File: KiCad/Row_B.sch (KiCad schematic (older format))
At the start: 14 parts, among them U101 RGB_WS2811B, U102 RGB_WS2811B, U103 RGB_WS2811B, U104 RGB_WS2811B, U105 RGB_WS2811B, U106 RGB_WS2811B, U107 RGB_WS2811B, U108 RGB_WS2811B

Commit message: Schematic updated
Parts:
- removed C101: 100n, TinyTiM_Lib:c_0805, symbol C2
- removed C117: 47u,8V, TinyTiM_Lib:c_2917, symbol C_POL_1
- removed S101, S102, S103, S104: CONN_1, TinyTiM_Lib:Screw, symbol CONN_1
- removed U101, U102, U103, U104, U105, U106, U107, U108: RGB_WS2811B, TinyTiM_Lib:RGB_WS2811B, symbol RGB_WS2811B
- added C18, C19, C20, C21, C22, C23, C24, C25, C26, C27, C28, C29, C30, C31: 100n, TinyTiM_Lib:c_0805, symbol C2
- added U17, U18, U19, U20, U21, U22, U23, U24, U25, U26, U27, U28, U29, U30: RGB_WS2812B, symbol RGB_WS2812B
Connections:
- net labels added: DI_B, DO_B
- net labels removed: A_02, A_03, A_04, A_05, A_06, A_07, A_08, A_09, DI_A, DO_A
- wire segments 49 -> 82
- no-connect marks 4 -> 0
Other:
- note removed: "Mounting Screws"

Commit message: Schematic updated
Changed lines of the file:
@@
 Sheet 3 14
 Title "ClockFOUR"
-Date "29 sep 2014"
+Date "30 sep 2014"
 Rev ""
 Comp "WyoLum"
@@
 5V
 $Comp
-L GND #PWR7
+L GND #PWR013
 U 1 1 542A9B80
 P 1350 2350
-F 0 "#PWR7" H 1350 2350 30  0001 C CNN
+F 0 "#PWR013" H 1350 2350 30  0001 C CNN
 F 1 "GND" H 1350 2280 30  0001 C CNN
 F 2 "" H 1350 2350 60  0001 C CNN
@@
 	1450 2300 1450 4650
 Wire Wire Line
-	1450 4650 10400 4650
-Wire Wire Line
 	2000 4650 2000 4550
 Wire Wire Line
@@
 Connection ~ 2000 4650
 Wire Wire Line
-	9000 4650 9000 4550
-Connection ~ 9000 4650
-Wire Wire Line
 	7600 4650 7600 4550
 Connection ~ 7600 4650
-Wire Wire Line
-	6200 4650 6200 4550
-Connection ~ 6200 4650
 Wire Wire Line
 	4800 4650 4800 4550
@@
 Connection ~ 3300 5050
 Connection ~ 3300 4650
+Connection ~ 10200 5050
+Connection ~ 10400 4650
+Wire Wire Line
+	9000 4550 9000 4650
+Connection ~ 9000 4650
+Wire Wire Line
+	1450 4650 10400 4650
+Wire Wire Line
+	6200 4550 6200 4650
+Connection ~ 6200 4650
+Connection ~ 1450 2300
 $EndSCHEMATC

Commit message: Schematic updated, board started
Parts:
- C25: renamed from C18; Field5 100nF, 25V -> 100n, 25V
- C27: renamed from C22; Field5 100nF, 25V -> 100n, 25V
- C29: renamed from C26; Field5 100nF, 25V -> 100n, 25V
- C31: renamed from C30; Field5 100nF, 25V -> 100n, 25V
- C33: renamed from C21; Field5 100nF, 25V -> 100n, 25V
- C35: renamed from C25; Field5 100nF, 25V -> 100n, 25V
- C37: renamed from C29; Field5 100nF, 25V -> 100n, 25V
- renumbered C20 to C26, C24 to C28, C28 to C30, C19 to C32, C23 to C34, C27 to C36, C31 to C38, U17 to U16, U19 to U17, U21 to U18, U23 to U19, U25 to U20, U27 to U21, U29 to U22, U18 to U23, U20 to U24, U22 to U25, U24 to U26, U26 to U27, U30 to U29
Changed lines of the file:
@@
 LIBS:contrib
 LIBS:valves
-LIBS:TinyTiM-cache
-LIBS:TiNA_sym
+LIBS:ClockFOUR
 LIBS:ClockFOUR-cache
 EELAYER 27 0
@@
 Sheet 3 14
 Title "ClockFOUR"
-Date "30 sep 2014"
+Date "1 oct 2014"
 Rev ""
 Comp "WyoLum"
@@
 5V
 $Comp
-L GND #PWR013
+L GND #PWR015
 U 1 1 542A9B80
 P 1350 2350
-F 0 "#PWR013" H 1350 2350 30  0001 C CNN
+F 0 "#PWR015" H 1350 2350 30  0001 C CNN
 F 1 "GND" H 1350 2280 30  0001 C CNN
 F 2 "" H 1350 2350 60  0001 C CNN
@@
 $EndComp
 $Comp
-L C2 C18
+L C2 C25
 U 1 1 542A9B8E
 P 1900 2500
-F 0 "C18" H 1925 2600 50  0000 L CNN
+F 0 "C25" H 1925 2600 50  0000 L CNN
 F 1 "100n" H 1925 2400 50  0000 L CNN
 F 2 "TinyTiM_Lib:c_0805" H 1900 2500 50  0001 C CNN
 F 3 "" H 1900 2500 60  0001 C CNN
 F 4 "CAP CER 0.1UF 25V 10% X7R 0805" H 1900 2700 60  0001 L CNN "Field4"
-F 5 "100nF, 25V" H 1900 2800 60  0001 L CNN "Field5"
+F 5 "100n, 25V" H 1900 2800 60  0001 L CNN "Field5"
 F 6 "Surface Mount, MLCC" H 1900 2900 60  0001 L CNN "Field6"
 F 7 "Kemet" H 1900 3000 60  0001 L CNN "Field7"
@@
 $EndComp
 $Comp
-L RGB_WS2812B U17
+L RGB_WS2812B U16
 U 1 1 542A9B94
 P 1725 1525
-F 0 "U17" V 1475 1525 60  0000 C CNN
+F 0 "U16" V 1475 1525 60  0000 C CNN
 F 1 "RGB_WS2812B" V 2125 1525 60  0000 C CNN
 F 2 "" H 1725 1525 60  0000 C CNN
@@
 $EndComp
 $Comp
-L RGB_WS2812B U19
+L RGB_WS2812B U17
 U 1 1 542A9B9A
 P 3125 1525
-F 0 "U19" V 2875 1525 60  0000 C CNN
+F 0 "U17" V 2875 1525 60  0000 C CNN
 F 1 "RGB_WS2812B" V 3525 1525 60  0000 C CNN
 F 2 "" H 3125 1525 60  0000 C CNN
@@
 $EndComp
 $Comp
-L RGB_WS2812B U21
+L RGB_WS2812B U18
 U 1 1 542A9BA0
 P 4525 1525
-F 0 "U21" V 4275 1525 60  0000 C CNN
+F 0 "U18" V 4275 1525 60  0000 C CNN
 F 1 "RGB_WS2812B" V 4925 1525 60  0000 C CNN
 F 2 "" H 4525 1525 60  0000 C CNN
@@
 $EndComp
 $Comp
-L RGB_WS2812B U23
+L RGB_WS2812B U19
 U 1 1 542A9BA6
 P 5925 1525
-F 0 "U23" V 5675 1525 60  0000 C CNN
+F 0 "U19" V 5675 1525 60  0000 C CNN
 F 1 "RGB_WS2812B" V 6325 1525 60  0000 C CNN
 F 2 "" H 5925 1525 60  0000 C CNN
@@
 $EndComp
 $Comp
-L RGB_WS2812B U25
+L RGB_WS2812B U20
 U 1 1 542A9BAC
 P 7325 1525
-F 0 "U25" V 7075 1525 60  0000 C CNN
+F 0 "U20" V 7075 1525 60  0000 C CNN
 F 1 "RGB_WS2812B" V 7725 1525 60  0000 C CNN
 F 2 "" H 7325 1525 60  0000 C CNN
@@
 $EndComp
 $Comp
-L RGB_WS2812B U27
+L RGB_WS2812B U21
 U 1 1 542A9BB2
 P 8725 1525
-F 0 "U27" V 8475 1525 60  0000 C CNN
+F 0 "U21" V 8475 1525 60  0000 C CNN
 F 1 "RGB_WS2812B" V 9125 1525 60  0000 C CNN
 F 2 "" H 8725 1525 60  0000 C CNN
@@
 $EndComp
 $Comp
-L RGB_WS2812B U29
+L RGB_WS2812B U22
 U 1 1 542A9BB8
 P 10125 1525
-F 0 "U29" V 9875 1525 60  0000 C CNN
+F 0 "U22" V 9875 1525 60  0000 C CNN
 F 1 "RGB_WS2812B" V 10525 1525 60  0000 C CNN
 F 2 "" H 10125 1525 60  0000 C CNN
@@
 $EndComp
 $Comp
-L RGB_WS2812B U18
+L RGB_WS2812B U23
 U 1 1 542A9BBE
 P 1725 3925
-F 0 "U18" V 1475 3925 60  0000 C CNN
+F 0 "U23" V 1475 3925 60  0000 C CNN
 F 1 "RGB_WS2812B" V 2125 3925 60  0000 C CNN
 F 2 "" H 1725 3925 60  0000 C CNN
@@
 $EndComp
 $Comp
-L RGB_WS2812B U20
+L RGB_WS2812B U24
 U 1 1 542A9BC4
 P 3125 3925
-F 0 "U20" V 2875 3925 60  0000 C CNN
+F 0 "U24" V 2875 3925 60  0000 C CNN
 F 1 "RGB_WS2812B" V 3525 3925 60  0000 C CNN
 F 2 "" H 3125 3925 60  0000 C CNN
@@
 $EndComp
 $Comp
-L RGB_WS2812B U22
+L RGB_WS2812B U25
 U 1 1 542A9BCA
 P 4525 3925
-F 0 "U22" V 4275 3925 60  0000 C CNN
+F 0 "U25" V 4275 3925 60  0000 C CNN
 F 1 "RGB_WS2812B" V 4925 3925 60  0000 C CNN
 F 2 "" H 4525 3925 60  0000 C CNN
@@
 $EndComp
 $Comp
-L RGB_WS2812B U24
+L RGB_WS2812B U26
 U 1 1 542A9BD0
 P 5925 3925
-F 0 "U24" V 5675 3925 60  0000 C CNN
+F 0 "U26" V 5675 3925 60  0000 C CNN
 F 1 "RGB_WS2812B" V 6325 3925 60  0000 C CNN
 F 2 "" H 5925 3925 60  0000 C CNN
@@
 $EndComp
 $Comp
-L RGB_WS2812B U26
+L RGB_WS2812B U27
 U 1 1 542A9BD6
 P 7325 3925
-F 0 "U26" V 7075 3925 60  0000 C CNN
+F 0 "U27" V 7075 3925 60  0000 C CNN
 F 1 "RGB_WS2812B" V 7725 3925 60  0000 C CNN
 F 2 "" H 7325 3925 60  0000 C CNN
@@
 $EndComp
 $Comp
-L RGB_WS2812B U30
+L RGB_WS2812B U29
 U 1 1 542A9BE2
 P 10125 3925
-F 0 "U30" V 9875 3925 60  0000 C CNN
+F 0 "U29" V 9875 3925 60  0000 C CNN
 F 1 "RGB_WS2812B" V 10525 3925 60  0000 C CNN
 F 2 "" H 10125 3925 60  0000 C CNN
@@
 Connection ~ 1800 2700
 $Comp
-L C2 C20
+L C2 C26
 U 1 1 542A9C3D
 P 3300 2500
-F 0 "C20" H 3325 2600 50  0000 L CNN
+F 0 "C26" H 3325 2600 50  0000 L CNN
 F 1 "100n" H 3325 2400 50  0000 L CNN
 F 2 "TinyTiM_Lib:c_0805" H 3300 2500 50  0001 C CNN
@@
 $EndComp
 $Comp
-L C2 C22
+L C2 C27
 U 1 1 542A9C4B
 P 4700 2500
-F 0 "C22" H 4725 2600 50  0000 L CNN
+F 0 "C27" H 4725 2600 50  0000 L CNN
 F 1 "100n" H 4725 2400 50  0000 L CNN
 F 2 "TinyTiM_Lib:c_0805" H 4700 2500 50  0001 C CNN
 F 3 "" H 4700 2500 60  0001 C CNN
 F 4 "CAP CER 0.1UF 25V 10% X7R 0805" H 4700 2700 60  0001 L CNN "Field4"
-F 5 "100nF, 25V" H 4700 2800 60  0001 L CNN "Field5"
+F 5 "100n, 25V" H 4700 2800 60  0001 L CNN "Field5"
 F 6 "Surface Mount, MLCC" H 4700 2900 60  0001 L CNN "Field6"
 F 7 "Kemet" H 4700 3000 60  0001 L CNN "Field7"
@@
 $EndComp
 $Comp
-L C2 C24
+L C2 C28
 U 1 1 542A9C59
 P 6100 2500
-F 0 "C24" H 6125 2600 50  0000 L CNN
+F 0 "C28" H 6125 2600 50  0000 L CNN
 F 1 "100n" H 6125 2400 50  0000 L CNN
 F 2 "TinyTiM_Lib:c_0805" H 6100 2500 50  0001 C CNN
@@
 $EndComp
 $Comp
-L C2 C26
+L C2 C29
 U 1 1 542A9C67
 P 7500 2500
-F 0 "C26" H 7525 2600 50  0000 L CNN
+F 0 "C29" H 7525 2600 50  0000 L CNN
 F 1 "100n" H 7525 2400 50  0000 L CNN
 F 2 "TinyTiM_Lib:c_0805" H 7500 2500 50  0001 C CNN
 F 3 "" H 7500 2500 60  0001 C CNN
 F 4 "CAP CER 0.1UF 25V 10% X7R 0805" H 7500 2700 60  0001 L CNN "Field4"
-F 5 "100nF, 25V" H 7500 2800 60  0001 L CNN "Field5"
+F 5 "100n, 25V" H 7500 2800 60  0001 L CNN "Field5"
 F 6 "Surface Mount, MLCC" H 7500 2900 60  0001 L CNN "Field6"
 F 7 "Kemet" H 7500 3000 60  0001 L CNN "Field7"
@@
 $EndComp
 $Comp
-L C2 C28
+L C2 C30
 U 1 1 542A9C75
 P 8900 2500
-F 0 "C28" H 8925 2600 50  0000 L CNN
+F 0 "C30" H 8925 2600 50  0000 L CNN
 F 1 "100n" H 8925 2400 50  0000 L CNN
 F 2 "TinyTiM_Lib:c_0805" H 8900 2500 50  0001 C CNN
@@
 $EndComp
 $Comp
-L C2 C30
+L C2 C31
 U 1 1 542A9C83
 P 10300 2500
-F 0 "C30" H 10325 2600 50  0000 L CNN
+F 0 "C31" H 10325 2600 50  0000 L CNN
 F 1 "100n" H 10325 2400 50  0000 L CNN
 F 2 "TinyTiM_Lib:c_0805" H 10300 2500 50  0001 C CNN
 F 3 "" H 10300 2500 60  0001 C CNN
 F 4 "CAP CER 0.1UF 25V 10% X7R 0805" H 10300 2700 60  0001 L CNN "Field4"
-F 5 "100nF, 25V" H 10300 2800 60  0001 L CNN "Field5"
+F 5 "100n, 25V" H 10300 2800 60  0001 L CNN "Field5"
 F 6 "Surface Mount, MLCC" H 10300 2900 60  0001 L CNN "Field6"
 F 7 "Kemet" H 10300 3000 60  0001 L CNN "Field7"
@@
 Connection ~ 10200 2700
 $Comp
-L C2 C19
+L C2 C32
 U 1 1 542A9C92
 P 1900 4850
-F 0 "C19" H 1925 4950 50  0000 L CNN
+F 0 "C32" H 1925 4950 50  0000 L CNN
 F 1 "100n" H 1925 4750 50  0000 L CNN
 F 2 "TinyTiM_Lib:c_0805" H 1900 4850 50  0001 C CNN
@@
 Connection ~ 1800 5050
 $Comp
-L C2 C21
+L C2 C33
 U 1 1 542A9CCF
 P 3300 4850
-F 0 "C21" H 3325 4950 50  0000 L CNN
+F 0 "C33" H 3325 4950 50  0000 L CNN
 F 1 "100n" H 3325 4750 50  0000 L CNN
 F 2 "TinyTiM_Lib:c_0805" H 3300 4850 50  0001 C CNN
 F 3 "" H 3300 4850 60  0001 C CNN
 F 4 "CAP CER 0.1UF 25V 10% X7R 0805" H 3300 5050 60  0001 L CNN "Field4"
-F 5 "100nF, 25V" H 3300 5150 60  0001 L CNN "Field5"
+F 5 "100n, 25V" H 3300 5150 60  0001 L CNN "Field5"
 F 6 "Surface Mount, MLCC" H 3300 5250 60  0001 L CNN "Field6"
 F 7 "Kemet" H 3300 5350 60  0001 L CNN "Field7"
@@
 $EndComp
 $Comp
-L C2 C23
+L C2 C34
 U 1 1 542A9CDD
 P 4700 4850
-F 0 "C23" H 4725 4950 50  0000 L CNN
+F 0 "C34" H 4725 4950 50  0000 L CNN
 F 1 "100n" H 4725 4750 50  0000 L CNN
 F 2 "TinyTiM_Lib:c_0805" H 4700 4850 50  0001 C CNN
@@
 $EndComp
 $Comp
-L C2 C25
+L C2 C35
 U 1 1 542A9CEB
 P 6100 4850
-F 0 "C25" H 6125 4950 50  0000 L CNN
+F 0 "C35" H 6125 4950 50  0000 L CNN
 F 1 "100n" H 6125 4750 50  0000 L CNN
 F 2 "TinyTiM_Lib:c_0805" H 6100 4850 50  0001 C CNN
 F 3 "" H 6100 4850 60  0001 C CNN
 F 4 "CAP CER 0.1UF 25V 10% X7R 0805" H 6100 5050 60  0001 L CNN "Field4"
-F 5 "100nF, 25V" H 6100 5150 60  0001 L CNN "Field5"
+F 5 "100n, 25V" H 6100 5150 60  0001 L CNN "Field5"
 F 6 "Surface Mount, MLCC" H 6100 5250 60  0001 L CNN "Field6"
 F 7 "Kemet" H 6100 5350 60  0001 L CNN "Field7"
@@
 $EndComp
 $Comp
-L C2 C27
+L C2 C36
 U 1 1 542A9CF9
 P 7500 4850
-F 0 "C27" H 7525 4950 50  0000 L CNN
+F 0 "C36" H 7525 4950 50  0000 L CNN
 F 1 "100n" H 7525 4750 50  0000 L CNN
 F 2 "TinyTiM_Lib:c_0805" H 7500 4850 50  0001 C CNN
@@
 $EndComp
 $Comp
-L C2 C29
+L C2 C37
 U 1 1 542A9D07
 P 8900 4850
-F 0 "C29" H 8925 4950 50  0000 L CNN
+F 0 "C37" H 8925 4950 50  0000 L CNN
 F 1 "100n" H 8925 4750 50  0000 L CNN
 F 2 "TinyTiM_Lib:c_0805" H 8900 4850 50  0001 C CNN
 F 3 "" H 8900 4850 60  0001 C CNN
 F 4 "CAP CER 0.1UF 25V 10% X7R 0805" H 8900 5050 60  0001 L CNN "Field4"
-F 5 "100nF, 25V" H 8900 5150 60  0001 L CNN "Field5"
+F 5 "100n, 25V" H 8900 5150 60  0001 L CNN "Field5"
 F 6 "Surface Mount, MLCC" H 8900 5250 60  0001 L CNN "Field6"
 F 7 "Kemet" H 8900 5350 60  0001 L CNN "Field7"
@@
 $EndComp
 $Comp
-L C2 C31
+L C2 C38
 U 1 1 542A9D15
 P 10300 4850
-F 0 "C31" H 10325 4950 50  0000 L CNN
+F 0 "C38" H 10325 4950 50  0000 L CNN
 F 1 "100n" H 10325 4750 50  0000 L CNN
 F 2 "TinyTiM_Lib:c_0805" H 10300 4850 50  0001 C CNN

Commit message: Board layout updated
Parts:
- removed U16, U17, U18, U19, U20, U21, U22, U23, U24, U25, U26, U27, U28, U29: RGB_WS2812B, symbol RGB_WS2812B
- added LED15, LED16, LED17, LED18, LED19, LED20, LED21, LED22, LED23, LED24, LED25, LED26, LED27, LED28: WS2812B, ~, symbol WS2812B

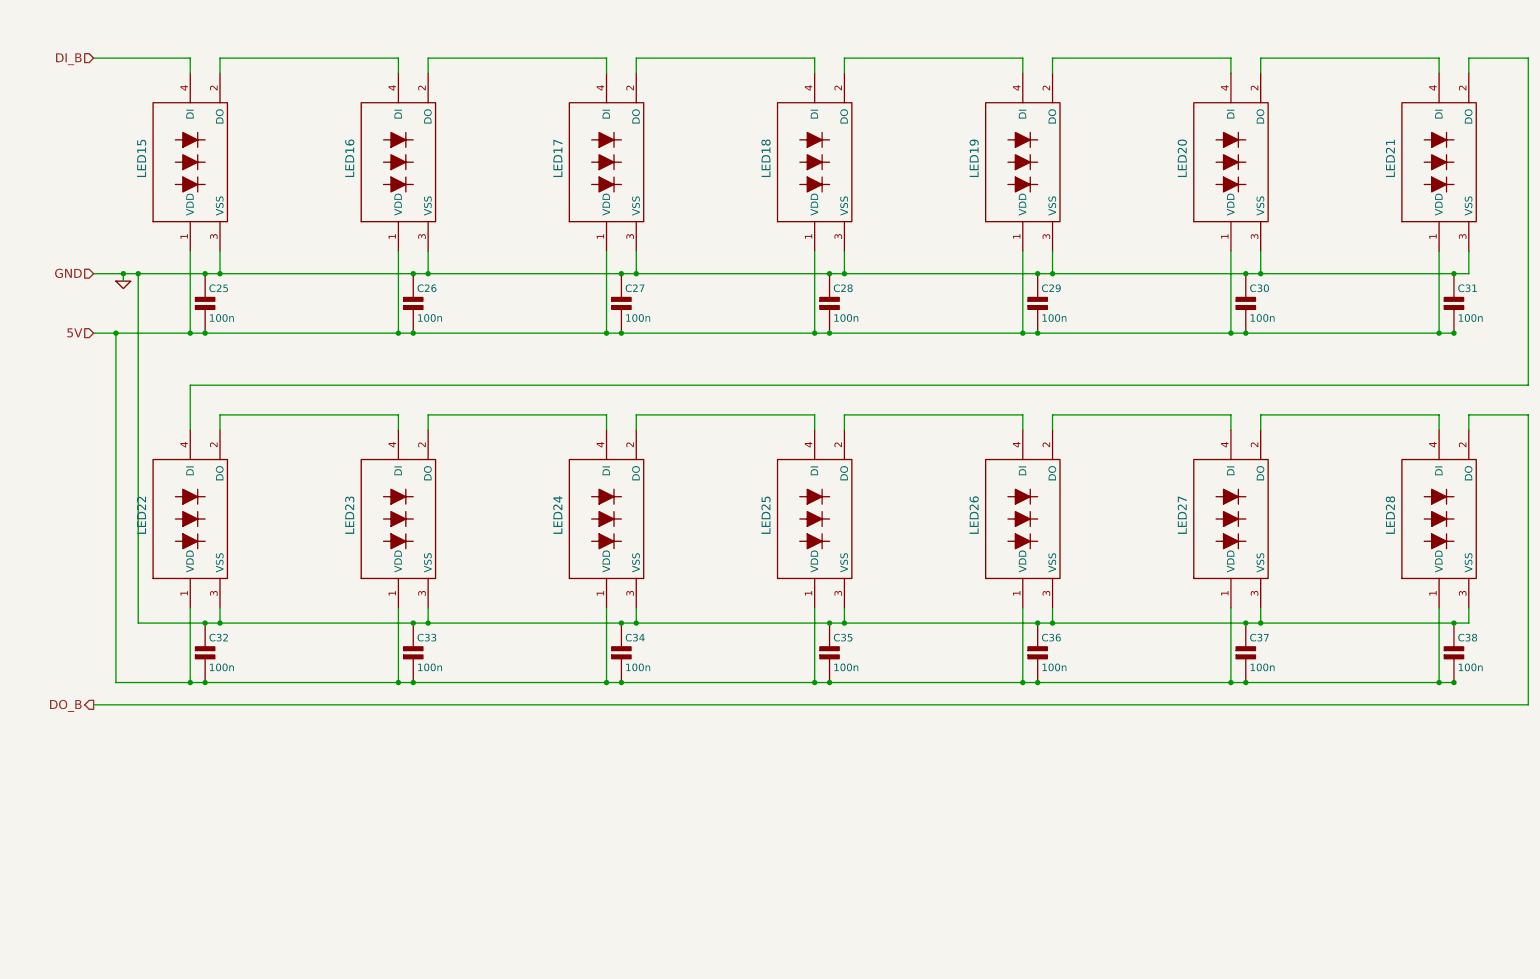
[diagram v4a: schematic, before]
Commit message: Board layout updated
Matrix placed and wired. Added RTC.
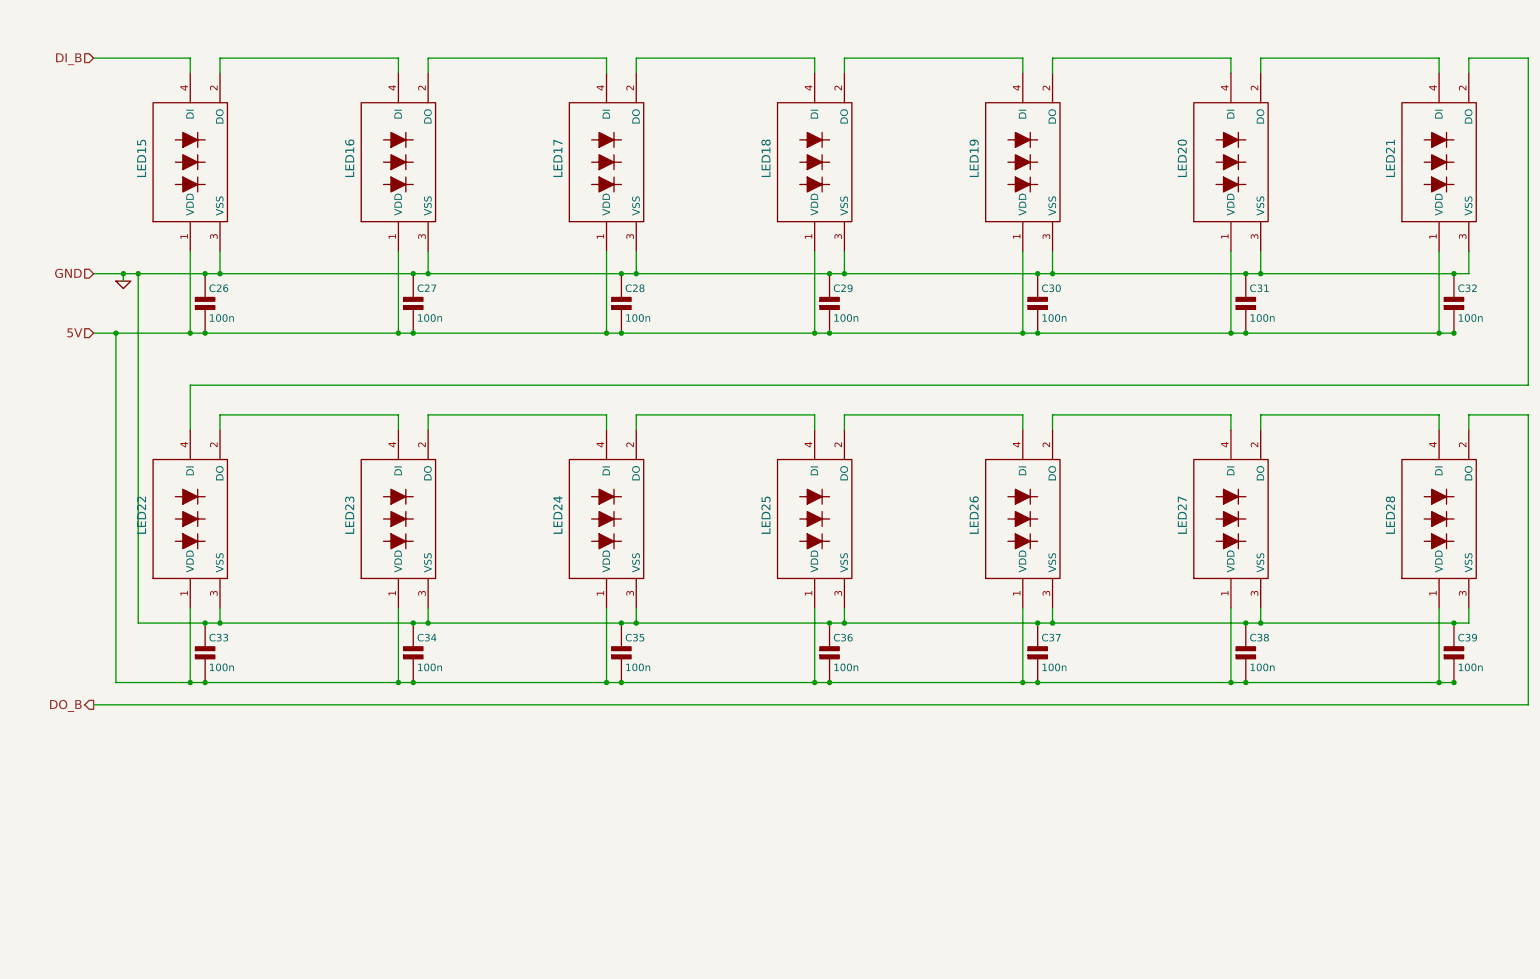
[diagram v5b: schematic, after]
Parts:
- renumbered C25 to C26, C26 to C27, C27 to C28, C28 to C29, C29 to C30, C30 to C31, C31 to C32, C32 to C33, C33 to C34, C34 to C35, C35 to C36, C36 to C37, C37 to C38, C38 to C39
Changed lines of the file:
@@
 Sheet 3 14
 Title "ClockFOUR"
-Date "2 oct 2014"
+Date "3 oct 2014"
 Rev ""
 Comp "WyoLum"
@@
 $EndComp
 $Comp
-L C2 C25
+L C2 C26
 U 1 1 542DEF34
 P 1900 2750
-F 0 "C25" H 1925 2850 50  0000 L CNN
+F 0 "C26" H 1925 2850 50  0000 L CNN
 F 1 "100n" H 1925 2650 50  0000 L CNN
 F 2 "TinyTiM_Lib:c_0805" H 1900 2750 50  0001 C CNN
@@
 Connection ~ 1800 2950
 $Comp
-L C2 C26
+L C2 C27
 U 1 1 542DEF8F
 P 3300 2750
-F 0 "C26" H 3325 2850 50  0000 L CNN
+F 0 "C27" H 3325 2850 50  0000 L CNN
 F 1 "100n" H 3325 2650 50  0000 L CNN
 F 2 "TinyTiM_Lib:c_0805" H 3300 2750 50  0001 C CNN
@@
 $EndComp
 $Comp
-L C2 C27
+L C2 C28
 U 1 1 542DEF9D
 P 4700 2750
-F 0 "C27" H 4725 2850 50  0000 L CNN
+F 0 "C28" H 4725 2850 50  0000 L CNN
 F 1 "100n" H 4725 2650 50  0000 L CNN
 F 2 "TinyTiM_Lib:c_0805" H 4700 2750 50  0001 C CNN
@@
 $EndComp
 $Comp
-L C2 C28
+L C2 C29
 U 1 1 542DEFAB
 P 6100 2750
-F 0 "C28" H 6125 2850 50  0000 L CNN
+F 0 "C29" H 6125 2850 50  0000 L CNN
 F 1 "100n" H 6125 2650 50  0000 L CNN
 F 2 "TinyTiM_Lib:c_0805" H 6100 2750 50  0001 C CNN
@@
 $EndComp
 $Comp
-L C2 C29
+L C2 C30
 U 1 1 542DEFB9
 P 7500 2750
-F 0 "C29" H 7525 2850 50  0000 L CNN
+F 0 "C30" H 7525 2850 50  0000 L CNN
 F 1 "100n" H 7525 2650 50  0000 L CNN
 F 2 "TinyTiM_Lib:c_0805" H 7500 2750 50  0001 C CNN
@@
 $EndComp
 $Comp
-L C2 C30
+L C2 C31
 U 1 1 542DEFC7
 P 8900 2750
-F 0 "C30" H 8925 2850 50  0000 L CNN
+F 0 "C31" H 8925 2850 50  0000 L CNN
 F 1 "100n" H 8925 2650 50  0000 L CNN
 F 2 "TinyTiM_Lib:c_0805" H 8900 2750 50  0001 C CNN
@@
 $EndComp
 $Comp
-L C2 C31
+L C2 C32
 U 1 1 542DEFD5
 P 10300 2750
-F 0 "C31" H 10325 2850 50  0000 L CNN
+F 0 "C32" H 10325 2850 50  0000 L CNN
 F 1 "100n" H 10325 2650 50  0000 L CNN
 F 2 "TinyTiM_Lib:c_0805" H 10300 2750 50  0001 C CNN
@@
 Connection ~ 10200 2950
 $Comp
-L C2 C32
+L C2 C33
 U 1 1 542DEFE4
 P 1900 5100
-F 0 "C32" H 1925 5200 50  0000 L CNN
+F 0 "C33" H 1925 5200 50  0000 L CNN
 F 1 "100n" H 1925 5000 50  0000 L CNN
 F 2 "TinyTiM_Lib:c_0805" H 1900 5100 50  0001 C CNN
@@
 Connection ~ 1800 5300
 $Comp
-L C2 C33
+L C2 C34
 U 1 1 542DF021
 P 3300 5100
-F 0 "C33" H 3325 5200 50  0000 L CNN
+F 0 "C34" H 3325 5200 50  0000 L CNN
 F 1 "100n" H 3325 5000 50  0000 L CNN
 F 2 "TinyTiM_Lib:c_0805" H 3300 5100 50  0001 C CNN
@@
 $EndComp
 $Comp
-L C2 C34
+L C2 C35
 U 1 1 542DF02F
 P 4700 5100
-F 0 "C34" H 4725 5200 50  0000 L CNN
+F 0 "C35" H 4725 5200 50  0000 L CNN
 F 1 "100n" H 4725 5000 50  0000 L CNN
 F 2 "TinyTiM_Lib:c_0805" H 4700 5100 50  0001 C CNN
@@
 $EndComp
 $Comp
-L C2 C35
+L C2 C36
 U 1 1 542DF03D
 P 6100 5100
-F 0 "C35" H 6125 5200 50  0000 L CNN
+F 0 "C36" H 6125 5200 50  0000 L CNN
 F 1 "100n" H 6125 5000 50  0000 L CNN
 F 2 "TinyTiM_Lib:c_0805" H 6100 5100 50  0001 C CNN
@@
 $EndComp
 $Comp
-L C2 C36
+L C2 C37
 U 1 1 542DF04B
 P 7500 5100
-F 0 "C36" H 7525 5200 50  0000 L CNN
+F 0 "C37" H 7525 5200 50  0000 L CNN
 F 1 "100n" H 7525 5000 50  0000 L CNN
 F 2 "TinyTiM_Lib:c_0805" H 7500 5100 50  0001 C CNN
@@
 $EndComp
 $Comp
-L C2 C37
+L C2 C38
 U 1 1 542DF059
 P 8900 5100
-F 0 "C37" H 8925 5200 50  0000 L CNN
+F 0 "C38" H 8925 5200 50  0000 L CNN
 F 1 "100n" H 8925 5000 50  0000 L CNN
 F 2 "TinyTiM_Lib:c_0805" H 8900 5100 50  0001 C CNN
@@
 $EndComp
 $Comp
-L C2 C38
+L C2 C39
 U 1 1 542DF067
 P 10300 5100
-F 0 "C38" H 10325 5200 50  0000 L CNN
+F 0 "C39" H 10325 5200 50  0000 L CNN
 F 1 "100n" H 10325 5000 50  0000 L CNN
 F 2 "TinyTiM_Lib:c_0805" H 10300 5100 50  0001 C CNN
